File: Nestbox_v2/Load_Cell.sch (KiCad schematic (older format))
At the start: 29 parts, among them J601 LOAD_CELL_CONN_01X04, Q601 CSD23381F4, Q602 CSD13381F4, Q603 CSD23381F4, Q604 CSD13381F4, U601 ADS1220

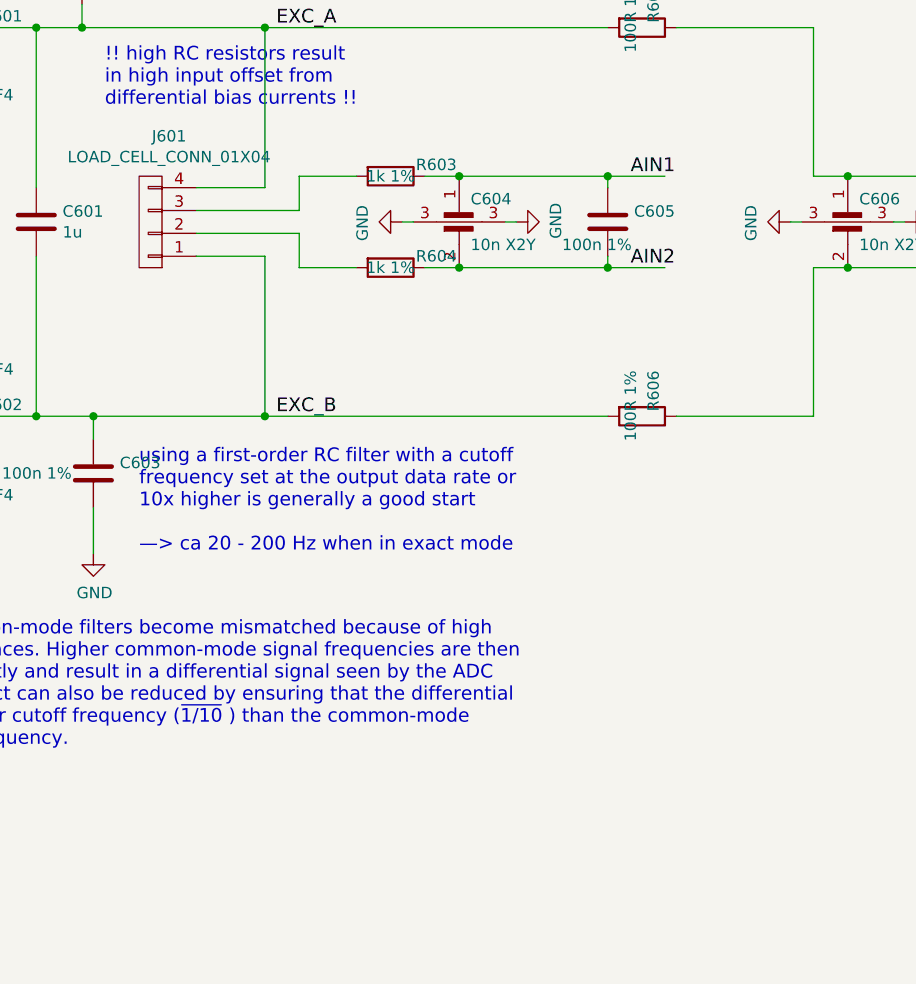
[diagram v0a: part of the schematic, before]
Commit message: all footprints assigned except mosfets; final connectors and their locatino, started component placement
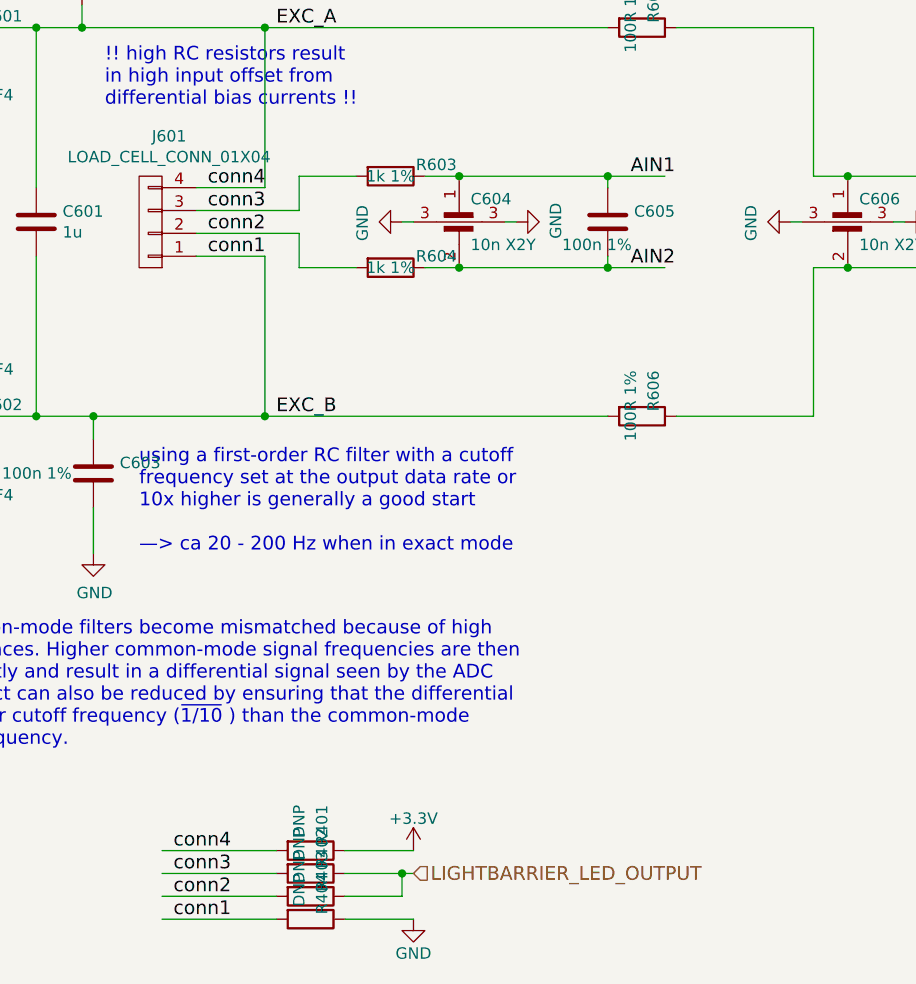
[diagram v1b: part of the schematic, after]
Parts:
- added R401, R402, R403, R404: DNP, Resistors_SMD:R_0603, symbol R
- J601: footprint Terminal_Blocks:TerminalBlock_Pheonix_PT-3.5mm_4pol -> Terminal_Blocks:TerminalBlock_Pheonix_MPT-2.54mm_4pol
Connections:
- net labels added: +3.3V, LIGHTBARRIER_LED_OUTPUT, conn1, conn2, conn3, conn4
- wire segments 77 -> 86
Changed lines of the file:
@@
 EESchema Schematic File Version 2
-LIBS:Nestbox_v2-rescue
-LIBS:Octanis3
 LIBS:power
 LIBS:device
-LIBS:switches
-LIBS:relays
-LIBS:motors
 LIBS:transistors
 LIBS:conn
@@
 LIBS:contrib
 LIBS:valves
-LIBS:SeeedOPL-Capacitor-2016
-LIBS:SeeedOPL-Connector-2016
-LIBS:SeeedOPL-Crystal Oscillator-2016
-LIBS:SeeedOPL-Diode-2016
-LIBS:SeeedOPL-Display-2016
-LIBS:SeeedOPL-Fuse-2016
-LIBS:SeeedOPL-IC-2016
-LIBS:SeeedOPL-Inductor-2016
-LIBS:SeeedOPL-LED-2016
-LIBS:SeeedOPL-Relay-2016
-LIBS:SeeedOPL-Resistor-2016
-LIBS:SeeedOPL-Sensor-2016
-LIBS:SeeedOPL-Switch-2016
-LIBS:SeeedOPL-Transistor-2016
+LIBS:Octanis3
 LIBS:Nestbox_v2-cache
 EELAYER 25 0
@@
 $EndDescr
 $Comp
-L +3V3 #PWR613
+L +3V3 #PWR050
 U 1 1 5AF731D8
 P 7950 2900
-F 0 "#PWR613" H 7950 2750 50  0001 C CNN
+F 0 "#PWR050" H 7950 2750 50  0001 C CNN
 F 1 "+3V3" H 7965 3073 50  0000 C CNN
 F 2 "" H 7950 2900 50  0001 C CNN
@@
 $EndComp
 $Comp
-L GND #PWR614
+L GND #PWR051
 U 1 1 5AF734D9
 P 7950 4600
-F 0 "#PWR614" H 7950 4350 50  0001 C CNN
+F 0 "#PWR051" H 7950 4350 50  0001 C CNN
 F 1 "GND" H 7955 4427 50  0000 C CNN
 F 2 "" H 7950 4600 50  0001 C CNN
@@
 $EndComp
 $Comp
-L GND #PWR616
+L GND #PWR052
 U 1 1 5AF737C3
 P 8050 4600
-F 0 "#PWR616" H 8050 4350 50  0001 C CNN
+F 0 "#PWR052" H 8050 4350 50  0001 C CNN
 F 1 "GND" H 8055 4427 50  0000 C CNN
 F 2 "" H 8050 4600 50  0001 C CNN
@@
 $EndComp
 $Comp
-L GND #PWR617
+L GND #PWR053
 U 1 1 5AF737DA
 P 8650 3100
-F 0 "#PWR617" H 8650 2850 50  0001 C CNN
+F 0 "#PWR053" H 8650 2850 50  0001 C CNN
 F 1 "GND" V 8655 2972 50  0000 R CNN
 F 2 "" H 8650 3100 50  0001 C CNN
@@
 $EndComp
 $Comp
-L GND #PWR618
+L GND #PWR054
 U 1 1 5AF73803
 P 8650 3350
-F 0 "#PWR618" H 8650 3100 50  0001 C CNN
+F 0 "#PWR054" H 8650 3100 50  0001 C CNN
 F 1 "GND" V 8655 3222 50  0000 R CNN
 F 2 "" H 8650 3350 50  0001 C CNN
@@
 $EndComp
 $Comp
-L GND #PWR612
+L GND #PWR055
 U 1 1 5AF73B67
 P 7450 3400
-F 0 "#PWR612" H 7450 3150 50  0001 C CNN
+F 0 "#PWR055" H 7450 3150 50  0001 C CNN
 F 1 "GND" V 7455 3272 50  0000 R CNN
 F 2 "" H 7450 3400 50  0001 C CNN
@@
 $EndComp
 $Comp
-L GND #PWR611
+L GND #PWR056
 U 1 1 5AF73BBF
 P 7450 3100
-F 0 "#PWR611" H 7450 2850 50  0001 C CNN
+F 0 "#PWR056" H 7450 2850 50  0001 C CNN
 F 1 "GND" V 7455 2972 50  0000 R CNN
 F 2 "" H 7450 3100 50  0001 C CNN
@@
 $EndComp
 $Comp
-L GND #PWR608
+L GND #PWR057
 U 1 1 5AF756EC
 P 4400 4000
-F 0 "#PWR608" H 4400 3750 50  0001 C CNN
+F 0 "#PWR057" H 4400 3750 50  0001 C CNN
 F 1 "GND" H 4405 3827 50  0000 C CNN
 F 2 "" H 4400 4000 50  0001 C CNN
@@
 $EndComp
 $Comp
-L GND #PWR607
+L GND #PWR058
 U 1 1 5AF75761
 P 3900 4000
-F 0 "#PWR607" H 3900 3750 50  0001 C CNN
+F 0 "#PWR058" H 3900 3750 50  0001 C CNN
 F 1 "GND" H 3905 3827 50  0000 C CNN
 F 2 "" H 3900 4000 50  0001 C CNN
@@
 F 0 "J601" H 2719 3625 50  0000 C CNN
 F 1 "LOAD_CELL_CONN_01X04" H 2719 3716 50  0000 C CNN
-F 2 "Terminal_Blocks:TerminalBlock_Pheonix_PT-3.5mm_4pol" H 2800 4000 50  0001 C CNN
+F 2 "Terminal_Blocks:TerminalBlock_Pheonix_MPT-2.54mm_4pol" H 2800 4000 50  0001 C CNN
 F 3 "" H 2800 4000 50  0001 C CNN
 	1    2800 4000
@@
 $EndComp
 $Comp
-L GND #PWR619
+L GND #PWR059
 U 1 1 5AF76892
 P 8800 4350
-F 0 "#PWR619" H 8800 4100 50  0001 C CNN
+F 0 "#PWR059" H 8800 4100 50  0001 C CNN
 F 1 "GND" H 8805 4177 50  0000 C CNN
 F 2 "" H 8800 4350 50  0001 C CNN
@@
 $EndComp
 $Comp
-L GND #PWR602
+L GND #PWR060
 U 1 1 5AF8B9E6
 P 1650 3750
-F 0 "#PWR602" H 1650 3500 50  0001 C CNN
+F 0 "#PWR060" H 1650 3500 50  0001 C CNN
 F 1 "GND" H 1655 3577 50  0000 C CNN
 F 2 "" H 1650 3750 50  0001 C CNN
@@
 $EndComp
 $Comp
-L GND #PWR604
+L GND #PWR061
 U 1 1 5AF8BA1F
 P 1650 5450
-F 0 "#PWR604" H 1650 5200 50  0001 C CNN
+F 0 "#PWR061" H 1650 5200 50  0001 C CNN
 F 1 "GND" H 1655 5277 50  0000 C CNN
 F 2 "" H 1650 5450 50  0001 C CNN
@@
 $EndComp
 $Comp
-L VAA #PWR601
+L VAA #PWR062
 U 1 1 5AF8BE8C
 P 1650 2600
-F 0 "#PWR601" H 1650 2450 50  0001 C CNN
+F 0 "#PWR062" H 1650 2450 50  0001 C CNN
 F 1 "VAA" H 1667 2773 50  0000 C CNN
 F 2 "" H 1650 2600 50  0001 C CNN
@@
 $EndComp
 $Comp
-L VAA #PWR603
+L VAA #PWR063
 U 1 1 5AF8C0F0
 P 1650 4250
-F 0 "#PWR603" H 1650 4100 50  0001 C CNN
+F 0 "#PWR063" H 1650 4100 50  0001 C CNN
 F 1 "VAA" H 1667 4423 50  0000 C CNN
 F 2 "" H 1650 4250 50  0001 C CNN
@@
 $EndComp
 $Comp
-L VAA #PWR615
+L VAA #PWR064
 U 1 1 5AF8C129
 P 8050 2550
-F 0 "#PWR615" H 8050 2400 50  0001 C CNN
+F 0 "#PWR064" H 8050 2400 50  0001 C CNN
 F 1 "VAA" H 8067 2723 50  0000 C CNN
 F 2 "" H 8050 2550 50  0001 C CNN
@@
 $EndComp
 $Comp
-L GND #PWR606
+L GND #PWR065
 U 1 1 5AF8D573
 P 2550 5450
-F 0 "#PWR606" H 2550 5200 50  0001 C CNN
+F 0 "#PWR065" H 2550 5200 50  0001 C CNN
 F 1 "GND" H 2555 5277 50  0000 C CNN
 F 2 "" H 2550 5450 50  0001 C CNN
@@
 $EndComp
 $Comp
-L GND #PWR605
+L GND #PWR066
 U 1 1 5AF8D7AF
 P 2500 2550
-F 0 "#PWR605" H 2500 2300 50  0001 C CNN
+F 0 "#PWR066" H 2500 2300 50  0001 C CNN
 F 1 "GND" H 2505 2377 50  0000 C CNN
 F 2 "" H 2500 2550 50  0001 C CNN
@@
 $EndComp
 $Comp
-L GND #PWR610
+L GND #PWR067
 U 1 1 5AF97D06
 P 6100 4000
-F 0 "#PWR610" H 6100 3750 50  0001 C CNN
+F 0 "#PWR067" H 6100 3750 50  0001 C CNN
 F 1 "GND" H 6105 3827 50  0000 C CNN
 F 2 "" H 6100 4000 50  0001 C CNN
@@
 $EndComp
 $Comp
-L GND #PWR609
+L GND #PWR068
 U 1 1 5AF97F53
 P 5600 4000
-F 0 "#PWR609" H 5600 3750 50  0001 C CNN
+F 0 "#PWR068" H 5600 3750 50  0001 C CNN
 F 1 "GND" H 5605 3827 50  0000 C CNN
 F 2 "" H 5600 4000 50  0001 C CNN
@@
 Text HLabel 1250 4600 0    60   Input ~ 0
 EXC_B_P
+Text Label 3050 4150 0    60   ~ 0
+conn1
+Text Label 3050 4050 0    60   ~ 0
+conn2
+Text Label 3050 3950 0    60   ~ 0
+conn3
+Text Label 3050 3850 0    60   ~ 0
+conn4
+Wire Wire Line
+	3350 6750 2850 6750
+Wire Wire Line
+	2850 6850 3350 6850
+Wire Wire Line
+	2850 6950 3350 6950
+Wire Wire Line
+	2850 7050 3350 7050
+Text Label 2900 7050 0    60   ~ 0
+conn1
+Text Label 2900 6950 0    60   ~ 0
+conn2
+Text Label 2900 6850 0    60   ~ 0
+conn3
+Text Label 2900 6750 0    60   ~ 0
+conn4
+$Comp
+L R R401
+U 1 1 5B1447CE
+P 3500 6750
+F 0 "R401" H 3300 6800 50  0000 L CNN
+F 1 "DNP" H 3300 6700 50  0000 L CNN
+F 2 "Resistors_SMD:R_0603" V 3430 6750 50  0001 C CNN
+F 3 "" H 3500 6750 50  0001 C CNN
+	1    3500 6750
+	0    1    1    0
+$EndComp
+$Comp
+L R R402
+U 1 1 5B14488A
+P 3500 6850
+F 0 "R402" H 3300 6900 50  0000 L CNN
+F 1 "DNP" H 3300 6800 50  0000 L CNN
+F 2 "Resistors_SMD:R_0603" V 3430 6850 50  0001 C CNN
+F 3 "" H 3500 6850 50  0001 C CNN
+	1    3500 6850
+	0    1    1    0
+$EndComp
+$Comp
+L R R403
+U 1 1 5B144B4E
+P 3500 6950
+F 0 "R403" H 3300 7000 50  0000 L CNN
+F 1 "DNP" H 3300 6900 50  0000 L CNN
+F 2 "Resistors_SMD:R_0603" V 3430 6950 50  0001 C CNN
+F 3 "" H 3500 6950 50  0001 C CNN
+	1    3500 6950
+	0    1    1    0
+$EndComp
+$Comp
+L R R404
+U 1 1 5B144C45
+P 3500 7050
+F 0 "R404" H 3300 7100 50  0000 L CNN
+F 1 "DNP" H 3300 7000 50  0000 L CNN
+F 2 "Resistors_SMD:R_0603" V 3430 7050 50  0001 C CNN
+F 3 "" H 3500 7050 50  0001 C CNN
+	1    3500 7050
+	0    1    1    0
+$EndComp
+Wire Wire Line
+	3650 6750 3950 6750
+Wire Wire Line
+	3650 6850 3950 6850
+Wire Wire Line
+	3900 6950 3650 6950
+Wire Wire Line
+	3900 6850 3900 6950
+Connection ~ 3900 6850
+Wire Wire Line
+	3650 7050 3950 7050
+Text HLabel 3950 6850 2    60   Input ~ 0
+LIGHTBARRIER_LED_OUTPUT
+$Comp
+L +3.3V #PWR069
+U 1 1 5B145174
+P 3950 6750
+F 0 "#PWR069" H 3950 6600 50  0001 C CNN
+F 1 "+3.3V" H 3950 6890 50  0000 C CNN
+F 2 "" H 3950 6750 50  0001 C CNN
+F 3 "" H 3950 6750 50  0001 C CNN
+	1    3950 6750
+	1    0    0    -1
+$EndComp
+$Comp
+L GND #PWR070
+U 1 1 5B14520C
+P 3950 7050
+F 0 "#PWR070" H 3950 6800 50  0001 C CNN
+F 1 "GND" H 3950 6900 50  0000 C CNN
+F 2 "" H 3950 7050 50  0001 C CNN
+F 3 "" H 3950 7050 50  0001 C CNN
+	1    3950 7050
+	1    0    0    -1
+$EndComp
 $EndSCHEMATC

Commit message: finished component placement
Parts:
- C604, C606: footprint murata-filter:NFM18PS -> Octanis3:Capacitor_X2Y_603
- Q601, Q603: value CSD23381F4 -> DMG2301L-7; footprint (none) -> TO_SOT_Packages_SMD:TSOT-23
- Q602, Q604: value CSD13381F4 -> DMG3402L; footprint (none) -> TO_SOT_Packages_SMD:TSOT-23
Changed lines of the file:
@@
 $EndDescr
 $Comp
-L +3V3 #PWR050
+L +3V3 #PWR049
 U 1 1 5AF731D8
 P 7950 2900
-F 0 "#PWR050" H 7950 2750 50  0001 C CNN
+F 0 "#PWR049" H 7950 2750 50  0001 C CNN
 F 1 "+3V3" H 7965 3073 50  0000 C CNN
 F 2 "" H 7950 2900 50  0001 C CNN
@@
 $EndComp
 $Comp
-L GND #PWR051
+L GND #PWR050
 U 1 1 5AF734D9
 P 7950 4600
-F 0 "#PWR051" H 7950 4350 50  0001 C CNN
+F 0 "#PWR050" H 7950 4350 50  0001 C CNN
 F 1 "GND" H 7955 4427 50  0000 C CNN
 F 2 "" H 7950 4600 50  0001 C CNN
@@
 $EndComp
 $Comp
-L GND #PWR052
+L GND #PWR051
 U 1 1 5AF737C3
 P 8050 4600
-F 0 "#PWR052" H 8050 4350 50  0001 C CNN
+F 0 "#PWR051" H 8050 4350 50  0001 C CNN
 F 1 "GND" H 8055 4427 50  0000 C CNN
 F 2 "" H 8050 4600 50  0001 C CNN
@@
 $EndComp
 $Comp
-L GND #PWR053
+L GND #PWR052
 U 1 1 5AF737DA
 P 8650 3100
-F 0 "#PWR053" H 8650 2850 50  0001 C CNN
+F 0 "#PWR052" H 8650 2850 50  0001 C CNN
 F 1 "GND" V 8655 2972 50  0000 R CNN
 F 2 "" H 8650 3100 50  0001 C CNN
@@
 $EndComp
 $Comp
-L GND #PWR054
+L GND #PWR053
 U 1 1 5AF73803
 P 8650 3350
-F 0 "#PWR054" H 8650 3100 50  0001 C CNN
+F 0 "#PWR053" H 8650 3100 50  0001 C CNN
 F 1 "GND" V 8655 3222 50  0000 R CNN
 F 2 "" H 8650 3350 50  0001 C CNN
@@
 $EndComp
 $Comp
-L GND #PWR055
+L GND #PWR054
 U 1 1 5AF73B67
 P 7450 3400
-F 0 "#PWR055" H 7450 3150 50  0001 C CNN
+F 0 "#PWR054" H 7450 3150 50  0001 C CNN
 F 1 "GND" V 7455 3272 50  0000 R CNN
 F 2 "" H 7450 3400 50  0001 C CNN
@@
 $EndComp
 $Comp
-L GND #PWR056
+L GND #PWR055
 U 1 1 5AF73BBF
 P 7450 3100
-F 0 "#PWR056" H 7450 2850 50  0001 C CNN
+F 0 "#PWR055" H 7450 2850 50  0001 C CNN
 F 1 "GND" V 7455 2972 50  0000 R CNN
 F 2 "" H 7450 3100 50  0001 C CNN
@@
 $EndComp
 $Comp
-L GND #PWR057
+L GND #PWR056
 U 1 1 5AF756EC
 P 4400 4000
-F 0 "#PWR057" H 4400 3750 50  0001 C CNN
+F 0 "#PWR056" H 4400 3750 50  0001 C CNN
 F 1 "GND" H 4405 3827 50  0000 C CNN
 F 2 "" H 4400 4000 50  0001 C CNN
@@
 $EndComp
 $Comp
-L GND #PWR058
+L GND #PWR057
 U 1 1 5AF75761
 P 3900 4000
-F 0 "#PWR058" H 3900 3750 50  0001 C CNN
+F 0 "#PWR057" H 3900 3750 50  0001 C CNN
 F 1 "GND" H 3905 3827 50  0000 C CNN
 F 2 "" H 3900 4000 50  0001 C CNN
@@
 $EndComp
 $Comp
-L GND #PWR059
+L GND #PWR058
 U 1 1 5AF76892
 P 8800 4350
-F 0 "#PWR059" H 8800 4100 50  0001 C CNN
+F 0 "#PWR058" H 8800 4100 50  0001 C CNN
 F 1 "GND" H 8805 4177 50  0000 C CNN
 F 2 "" H 8800 4350 50  0001 C CNN
@@
 P 1550 3400
 F 0 "Q602" H 1755 3446 50  0000 L CNN
-F 1 "CSD13381F4" H 1755 3355 50  0000 L CNN
-F 2 "" H 1750 3500 50  0001 C CNN
+F 1 "DMG3402L" H 1755 3355 50  0000 L CNN
+F 2 "TO_SOT_Packages_SMD:TSOT-23" H 1750 3500 50  0001 C CNN
 F 3 "" H 1550 3400 50  0001 C CNN
 	1    1550 3400
@@
 P 1550 5150
 F 0 "Q604" H 1755 5196 50  0000 L CNN
-F 1 "CSD13381F4" H 1755 5105 50  0000 L CNN
-F 2 "" H 1750 5250 50  0001 C CNN
+F 1 "DMG3402L" H 1755 5105 50  0000 L CNN
+F 2 "TO_SOT_Packages_SMD:TSOT-23" H 1750 5250 50  0001 C CNN
 F 3 "" H 1550 5150 50  0001 C CNN
 	1    1550 5150
@@
 P 1550 4600
 F 0 "Q603" H 1756 4646 50  0000 L CNN
-F 1 "CSD23381F4" H 1756 4555 50  0000 L CNN
-F 2 "" H 1750 4700 50  0001 C CNN
+F 1 "DMG2301L-7" H 1756 4555 50  0000 L CNN
+F 2 "TO_SOT_Packages_SMD:TSOT-23" H 1750 4700 50  0001 C CNN
 F 3 "" H 1550 4600 50  0001 C CNN
 	1    1550 4600
@@
 P 1550 2900
 F 0 "Q601" H 1756 2946 50  0000 L CNN
-F 1 "CSD23381F4" H 1756 2855 50  0000 L CNN
-F 2 "" H 1750 3000 50  0001 C CNN
+F 1 "DMG2301L-7" H 1756 2855 50  0000 L CNN
+F 2 "TO_SOT_Packages_SMD:TSOT-23" H 1750 3000 50  0001 C CNN
 F 3 "" H 1550 2900 50  0001 C CNN
 	1    1550 2900
@@
 $EndComp
 $Comp
-L GND #PWR060
+L GND #PWR059
 U 1 1 5AF8B9E6
 P 1650 3750
-F 0 "#PWR060" H 1650 3500 50  0001 C CNN
+F 0 "#PWR059" H 1650 3500 50  0001 C CNN
 F 1 "GND" H 1655 3577 50  0000 C CNN
 F 2 "" H 1650 3750 50  0001 C CNN
@@
 $EndComp
 $Comp
-L GND #PWR061
+L GND #PWR060
 U 1 1 5AF8BA1F
 P 1650 5450
-F 0 "#PWR061" H 1650 5200 50  0001 C CNN
+F 0 "#PWR060" H 1650 5200 50  0001 C CNN
 F 1 "GND" H 1655 5277 50  0000 C CNN
 F 2 "" H 1650 5450 50  0001 C CNN
@@
 $EndComp
 $Comp
-L VAA #PWR062
+L VAA #PWR061
 U 1 1 5AF8BE8C
 P 1650 2600
-F 0 "#PWR062" H 1650 2450 50  0001 C CNN
+F 0 "#PWR061" H 1650 2450 50  0001 C CNN
 F 1 "VAA" H 1667 2773 50  0000 C CNN
 F 2 "" H 1650 2600 50  0001 C CNN
@@
 $EndComp
 $Comp
-L VAA #PWR063
+L VAA #PWR062
 U 1 1 5AF8C0F0
 P 1650 4250
-F 0 "#PWR063" H 1650 4100 50  0001 C CNN
+F 0 "#PWR062" H 1650 4100 50  0001 C CNN
 F 1 "VAA" H 1667 4423 50  0000 C CNN
 F 2 "" H 1650 4250 50  0001 C CNN
@@
 $EndComp
 $Comp
-L VAA #PWR064
+L VAA #PWR063
 U 1 1 5AF8C129
 P 8050 2550
-F 0 "#PWR064" H 8050 2400 50  0001 C CNN
+F 0 "#PWR063" H 8050 2400 50  0001 C CNN
 F 1 "VAA" H 8067 2723 50  0000 C CNN
 F 2 "" H 8050 2550 50  0001 C CNN
@@
 $EndComp
 $Comp
-L GND #PWR065
+L GND #PWR064
 U 1 1 5AF8D573
 P 2550 5450
-F 0 "#PWR065" H 2550 5200 50  0001 C CNN
+F 0 "#PWR064" H 2550 5200 50  0001 C CNN
 F 1 "GND" H 2555 5277 50  0000 C CNN
 F 2 "" H 2550 5450 50  0001 C CNN
@@
 $EndComp
 $Comp
-L GND #PWR066
+L GND #PWR065
 U 1 1 5AF8D7AF
 P 2500 2550
-F 0 "#PWR066" H 2500 2300 50  0001 C CNN
+F 0 "#PWR065" H 2500 2300 50  0001 C CNN
 F 1 "GND" H 2505 2377 50  0000 C CNN
 F 2 "" H 2500 2550 50  0001 C CNN
@@
 F 0 "C604" H 4200 4300 50  0000 L CNN
 F 1 "10n X2Y" H 4200 4100 50  0000 L CNN
-F 2 "murata-filter:NFM18PS" V 4150 4100 50  0001 C CNN
+F 2 "Octanis3:Capacitor_X2Y_603" V 4150 4100 50  0001 C CNN
 F 3 "" V 4150 4100 50  0001 C CNN
 	1    4150 4100
@@
 F 0 "C606" H 5900 4300 50  0000 L CNN
 F 1 "10n X2Y" H 5900 4100 50  0000 L CNN
-F 2 "murata-filter:NFM18PS" V 5850 4100 50  0001 C CNN
+F 2 "Octanis3:Capacitor_X2Y_603" V 5850 4100 50  0001 C CNN
 F 3 "" V 5850 4100 50  0001 C CNN
 	1    5850 4100
@@
 $EndComp
 $Comp
-L GND #PWR067
+L GND #PWR066
 U 1 1 5AF97D06
 P 6100 4000
-F 0 "#PWR067" H 6100 3750 50  0001 C CNN
+F 0 "#PWR066" H 6100 3750 50  0001 C CNN
 F 1 "GND" H 6105 3827 50  0000 C CNN
 F 2 "" H 6100 4000 50  0001 C CNN
@@
 $EndComp
 $Comp
-L GND #PWR068
+L GND #PWR067
 U 1 1 5AF97F53
 P 5600 4000
-F 0 "#PWR068" H 5600 3750 50  0001 C CNN
+F 0 "#PWR067" H 5600 3750 50  0001 C CNN
 F 1 "GND" H 5605 3827 50  0000 C CNN
 F 2 "" H 5600 4000 50  0001 C CNN
@@
 Connection ~ 6450 4200
 Wire Wire Line
-	3300 3850 3000 3850
+	3000 3850 3350 3850
 Wire Wire Line
 	3000 3950 3450 3950
@@
 	3000 4150 3300 4150
 Wire Wire Line
-	3300 4150 3300 4850
-Wire Wire Line
 	8650 4200 9750 4200
 Wire Wire Line
@@
 Wire Wire Line
 	8800 4300 8650 4300
-Wire Wire Line
-	3300 3150 3300 3850
 Wire Wire Line
 	2100 3150 4800 3150
@@
 Wire Wire Line
 	1650 4800 1650 4950
-Connection ~ 3300 4850
 Connection ~ 1650 4850
 Wire Wire Line
@@
 LIGHTBARRIER_LED_OUTPUT
 $Comp
-L +3.3V #PWR069
+L +3.3V #PWR068
 U 1 1 5B145174
 P 3950 6750
-F 0 "#PWR069" H 3950 6600 50  0001 C CNN
+F 0 "#PWR068" H 3950 6600 50  0001 C CNN
 F 1 "+3.3V" H 3950 6890 50  0000 C CNN
 F 2 "" H 3950 6750 50  0001 C CNN
@@
 $EndComp
 $Comp
-L GND #PWR070
+L GND #PWR069
 U 1 1 5B14520C
 P 3950 7050
-F 0 "#PWR070" H 3950 6800 50  0001 C CNN
+F 0 "#PWR069" H 3950 6800 50  0001 C CNN
 F 1 "GND" H 3950 6900 50  0000 C CNN
 F 2 "" H 3950 7050 50  0001 C CNN
@@
 	1    0    0    -1
 $EndComp
+Wire Wire Line
+	3350 3850 3350 4850
+Connection ~ 3350 4850
+Wire Wire Line
+	3300 4150 3300 3150
 $EndSCHEMATC
